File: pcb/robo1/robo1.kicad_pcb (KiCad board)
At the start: 2 copper layers, 122.2 x 76.9 mm, 34 parts, among them J1 Conn_02x05_Odd_Even, J2 Conn_02x05_Odd_Even, J3 Conn_01x04_Pin, J4 Conn_01x04_Pin, J5 Screw_Terminal_01x02, J6 Screw_Terminal_01x02, SW1 SW_Push, SW2 SW_Push, SW3 SW_Push, U1 Pico

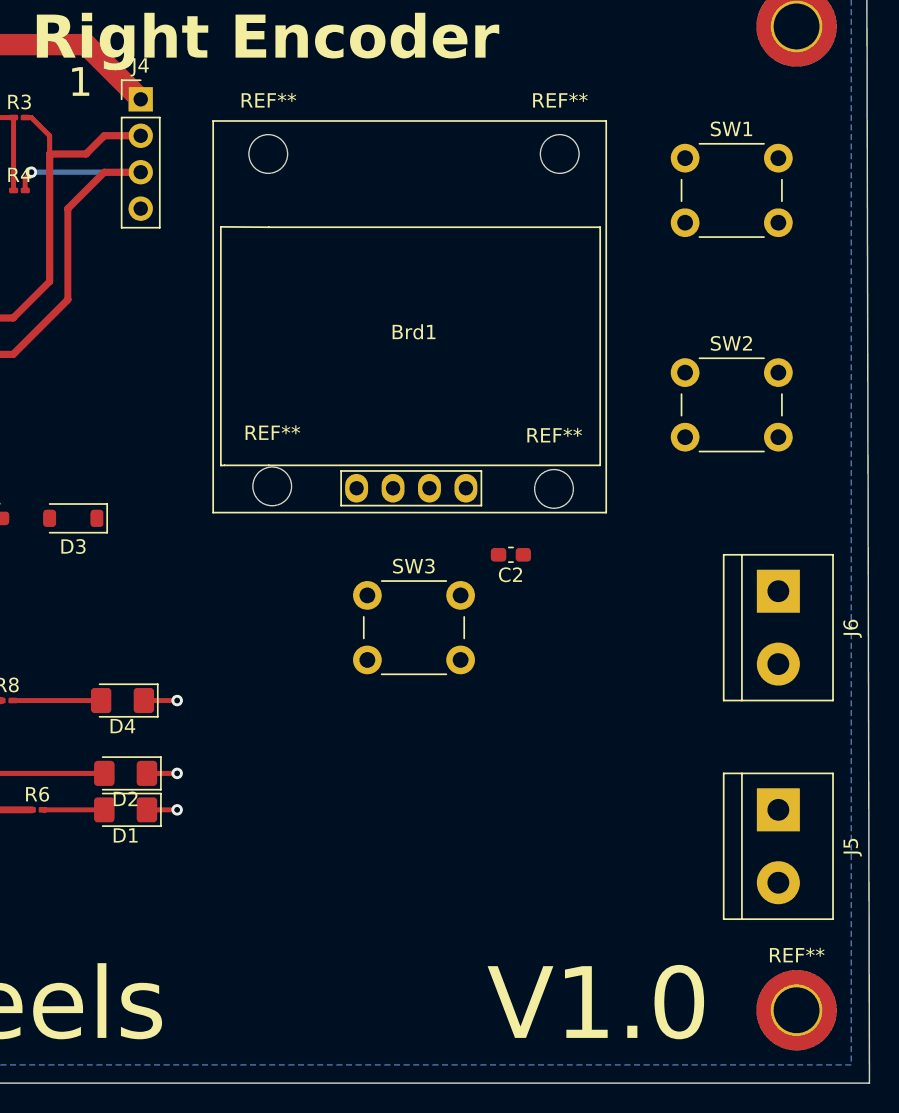
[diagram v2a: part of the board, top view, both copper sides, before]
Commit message: PCB added Isense connectors
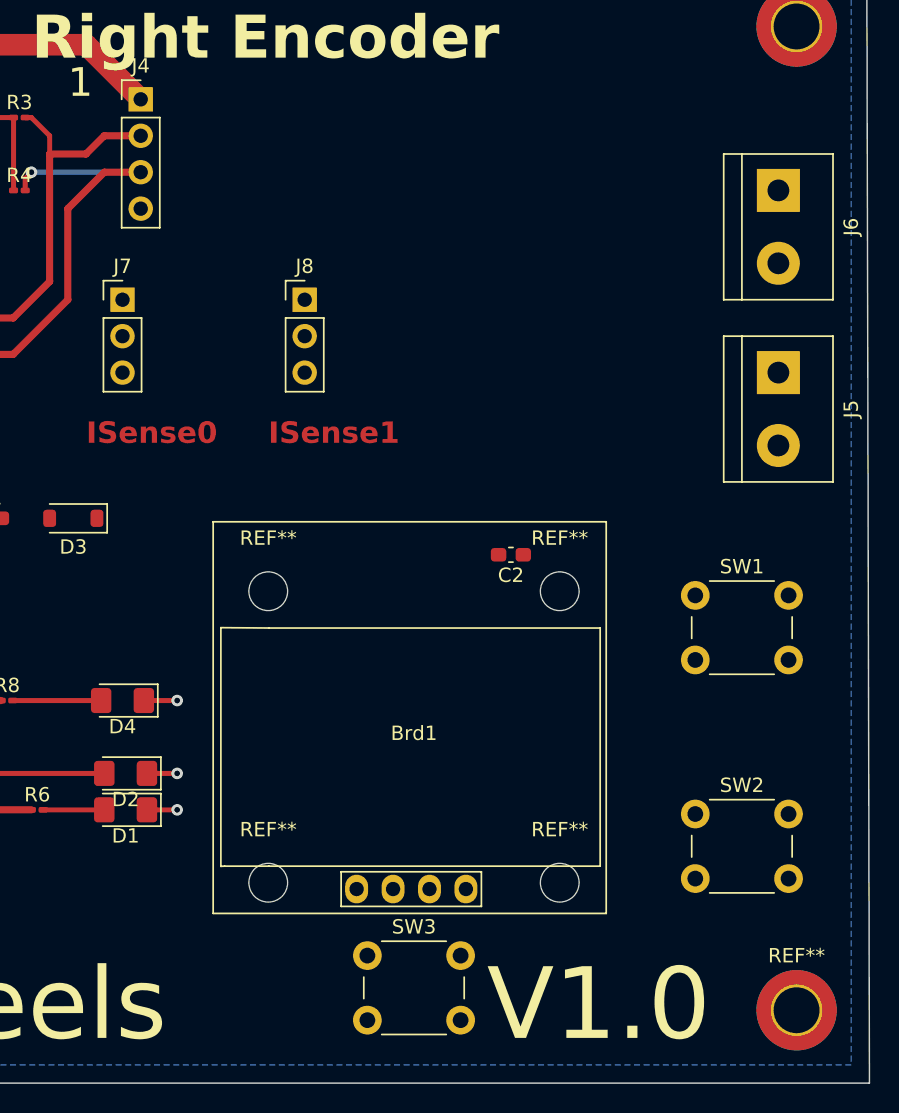
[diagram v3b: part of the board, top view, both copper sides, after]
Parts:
- added J7: Conn_01x03_Pin, Connector_PinHeader_2.54mm:PinHeader_1x03_P2.54mm_Vertical, F.Cu at (118.1, 67.3)
- added J8: Conn_01x03_Pin, Connector_PinHeader_2.54mm:PinHeader_1x03_P2.54mm_Vertical, F.Cu at (130.8, 67.3)
- moved SW2 30.8 mm to (158.0, 103.2)
- moved SW1 30.5 mm to (158.0, 87.9)
- moved J5 30.5 mm to (163.8, 72.4)
- moved REF** 30.5 mm to (148.6, 87.6)
- moved REF** 30.5 mm to (128.3, 87.6)
- moved Brd1 27.9 mm to (138.4, 97.8)
- moved J6 27.9 mm to (163.8, 59.7)
- moved REF** 27.6 mm to (128.3, 108.0)
- moved REF** 27.5 mm to (148.6, 108.0)
- moved SW3 25.1 mm to (135.2, 113.0)
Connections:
- J5 pad 1: unconnected-(J5-Pin_1-Pad1) -> +3.3V
- U1 pad 31: unconnected-(U1-GPIO26_ADC0-Pad31) -> Net-(J7-Pin_3)
- U1 pad 32: unconnected-(U1-GPIO27_ADC1-Pad32) -> Net-(J8-Pin_3)
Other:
- board text added: "ISense0"
- board text added: "ISense1"
